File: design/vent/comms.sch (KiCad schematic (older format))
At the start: 11 parts, among them J10 SD_Card_modified, U1 R-78E3.3-0.5, U2 SN74LVC2T45, U3 XBEE_SC1, U4 SN74LVC2T45, U5 SN74LVC2T45

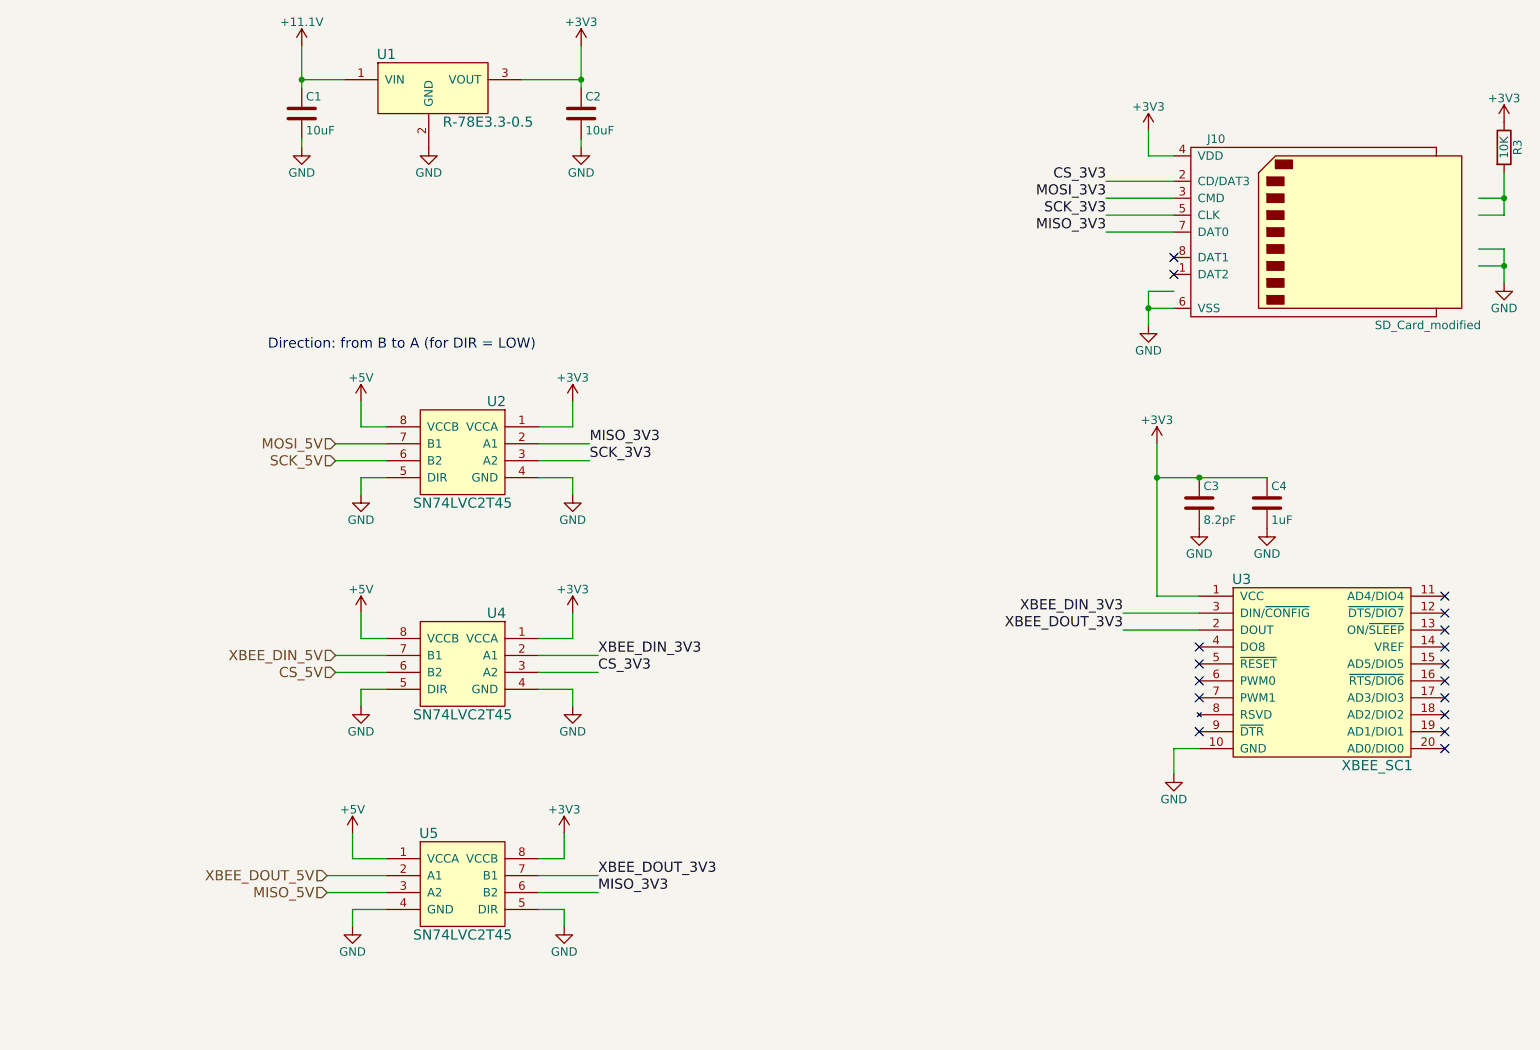
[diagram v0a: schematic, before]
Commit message: Refine schematic
- Add part numbers and correct pinout for mosfets
- Add fuses to battery inputs
- Add decoupling caps to logic translators
- Add flyback diodes to H Bridge, to be populated if the body diodes of
  the mosfets are not sufficient.
- Change H Bridge to operate with 4 inputs instead of 2.

Also, misc directory cleanup.
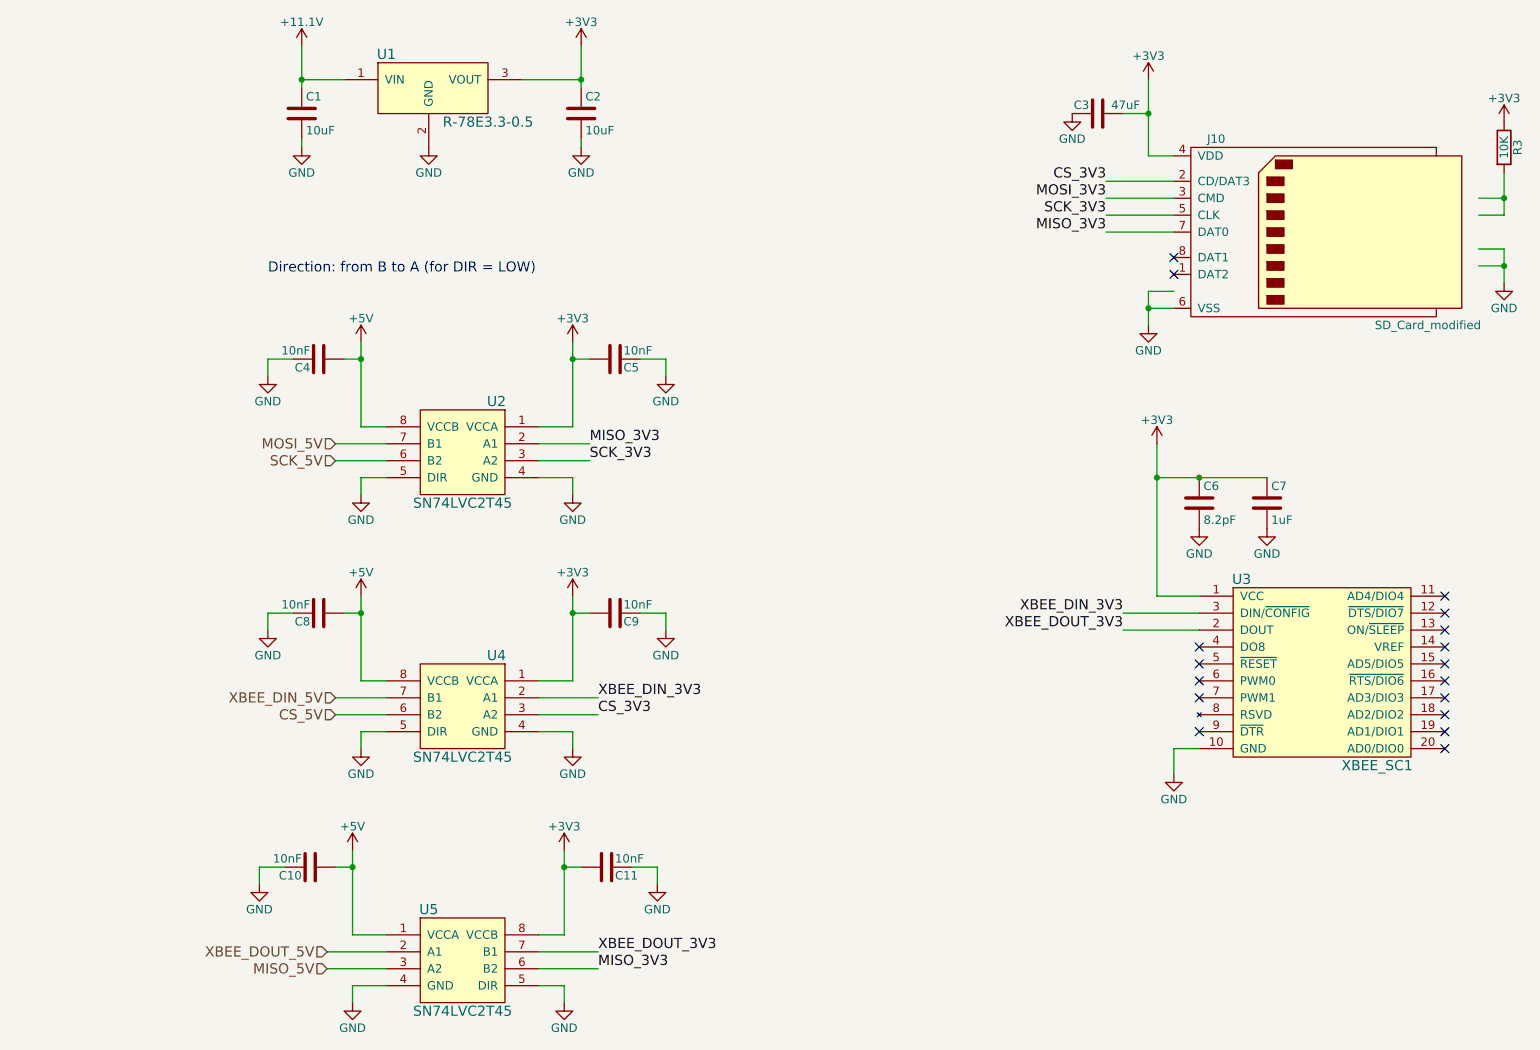
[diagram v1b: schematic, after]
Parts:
- added C10, C11, C4, C5, C8, C9: 10nF, symbol C
- added C3: 47uF, symbol C
- renumbered C3 to C6, C4 to C7
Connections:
- wire segments 64 -> 83
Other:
- moved on the sheet: U4, U5

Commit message: Review changes
- Add debug LEDs
- Add pullup resistors on logic shifters for xbee and sd card.
- Add 0 ohm resistor between valve and control power sources (to allow
  for either one of both sources to be used).
- Add another IMU
- Add gate resistors to valve control mosfets
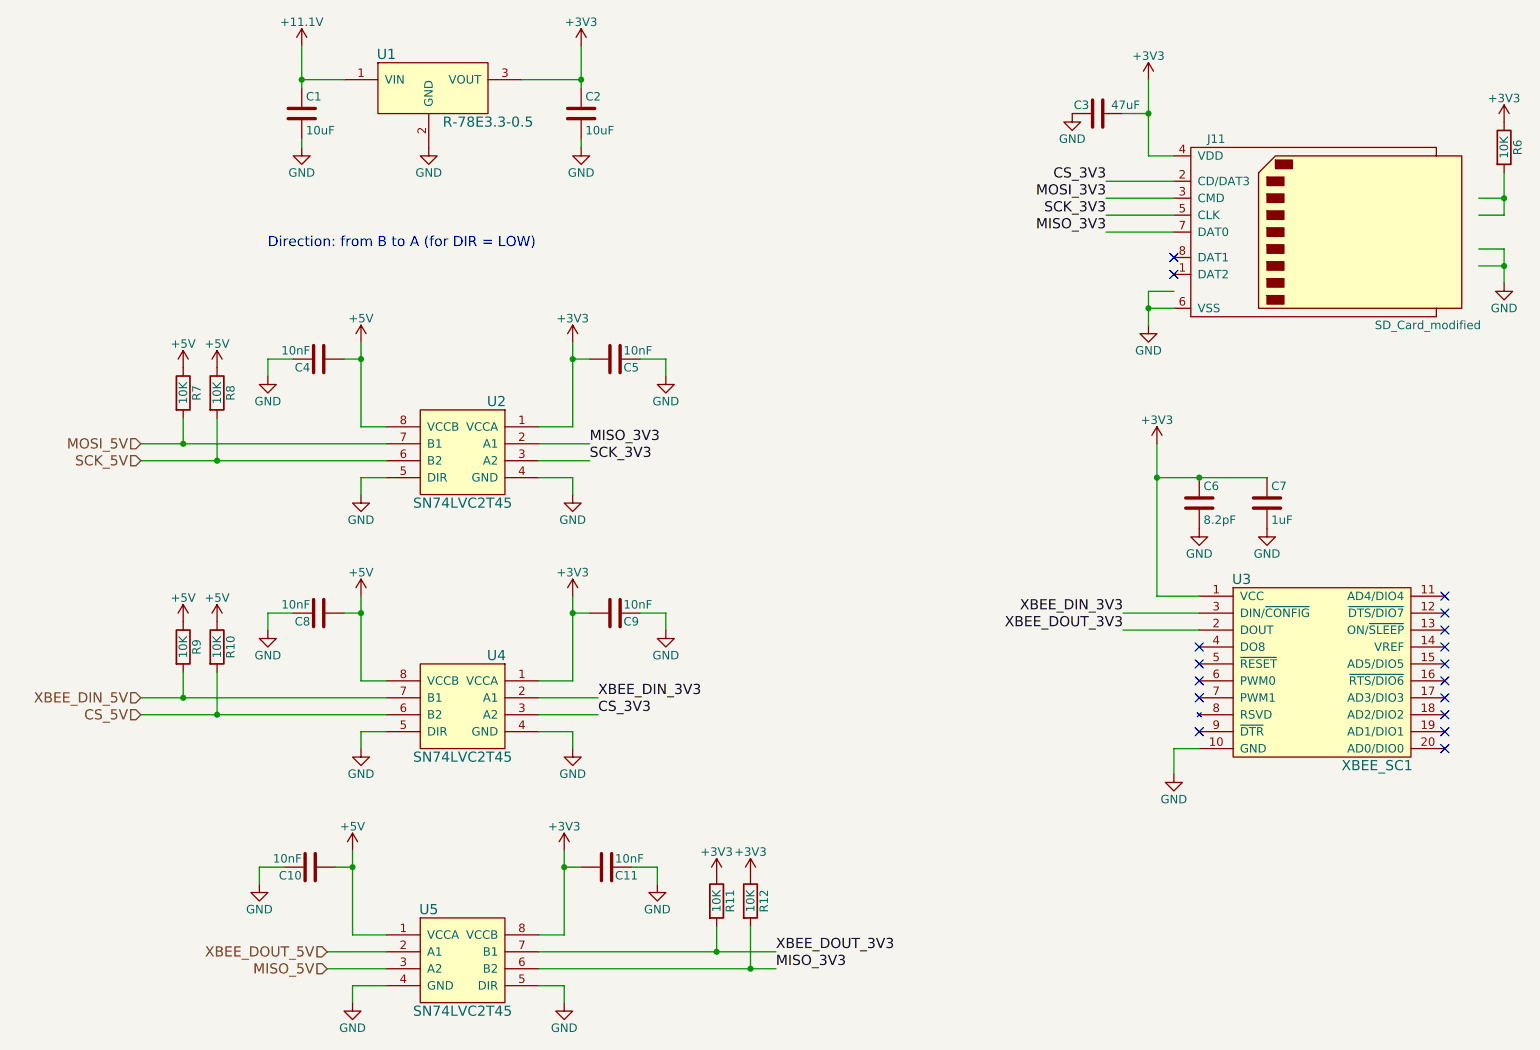
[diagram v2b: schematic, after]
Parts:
- added R10, R11, R12, R7, R8, R9: 10K, symbol R
- renumbered J10 to J11, R3 to R6
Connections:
- wire segments 83 -> 89

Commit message: Add connector part numbers to schematic
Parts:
- C1, C10, C11, C2, C3, C4, C5, C6, C7, C8, C9: footprint (none) -> Capacitors_SMD:C_0805_HandSoldering
- J11: footprint 10067847-001 -> (none)
- R10, R11, R12, R6, R7, R8, R9: footprint (none) -> Resistors_SMD:R_0805_HandSoldering
- U1: footprint (none) -> Package_SIP:SIP3_11.6x8.5mm
- U2, U4, U5: footprint (none) -> Housings_SSOP:TSSOP-8_3x3mm_Pitch0.65mm

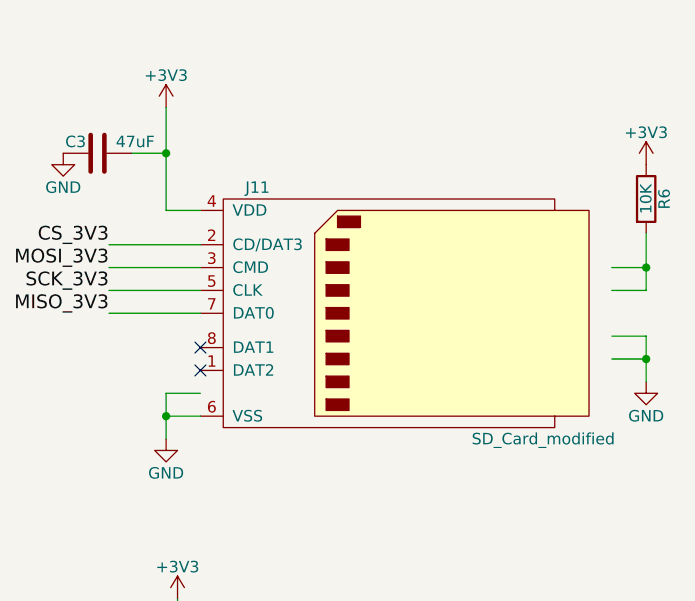
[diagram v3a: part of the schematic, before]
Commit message: Add more part numbers and footprints
- Flyback diodes
- Fuses
- Xbee
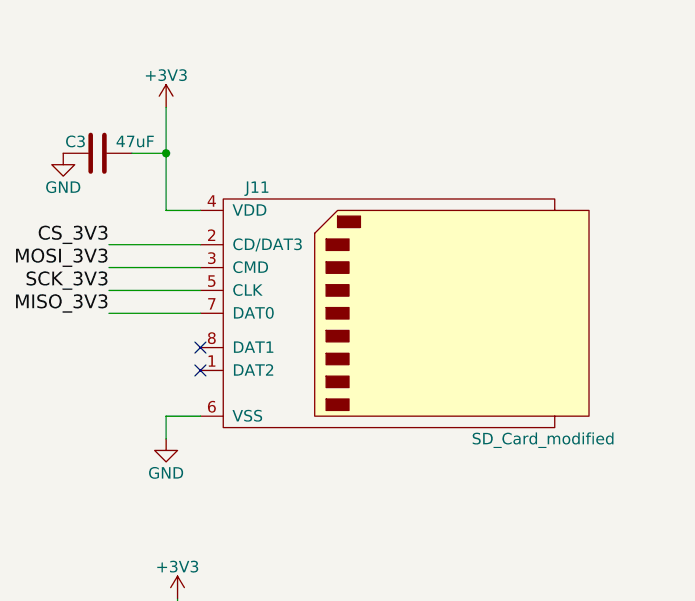
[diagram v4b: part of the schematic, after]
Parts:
- removed R6: 10K, Resistors_SMD:R_0805_HandSoldering, symbol R
- J11: footprint (none) -> Flight_Instr:WM6698CT-ND
- U3: footprint (none) -> Flight_Instr:Xbee_SC1
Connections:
- wire segments 89 -> 82
